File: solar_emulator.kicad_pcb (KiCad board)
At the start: 2 copper layers, 75 parts, among them J1 USB_C_Receptacle, J2 Conn_01x02, J3 Conn_01x03, J4 Conn_01x02, J5 Conn_01x02, J6 Conn_01x04, J7 Conn_01x02, Q1 IRFZ44N, Q2 IRFZ44N, Q3 IRFZ44N, Q4 IRFZ44N, Q5 IRFZ44N, Q6 IRFZ44N, Q7 IRFZ44N, Q8 IRFZ44N, SW1 SW_Push, SW2 SW_Push, U1 ESP32-S3-WROOM-1, U2 LD1117S33TR_SOT223, U3 HIP4081AIPZ, U4 LM393, U5 HIP4081AIPZ, U6 LM393

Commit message: implement footprints, begin placement of components
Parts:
- C2, C3: footprint Capacitor_THT:CP_Radial_D5.0mm_P2.00mm -> Capacitor_THT:C_Disc_D6.0mm_W2.5mm_P5.00mm
- moved C10 270.0 mm to (-162.8, 150.4)
- moved C11 270.0 mm to (-162.8, 154.4)
- moved C5 270.0 mm to (-162.8, 130.2)
- moved C6 270.0 mm to (-162.8, 134.2)
- moved C7 270.0 mm to (-162.8, 138.2)
- moved C8 270.0 mm to (-162.8, 142.3)
- moved C9 270.0 mm to (-162.8, 146.3)
- moved D1 270.0 mm to (-109.3, 130.9)
- moved D2 270.0 mm to (-109.3, 136.3)
- moved D3 270.0 mm to (-109.3, 141.8)
- moved D5 270.0 mm to (-123.1, 130.2)
- moved D6 270.0 mm to (-123.1, 134.5)
- moved D7 270.0 mm to (-123.1, 138.8)
- moved D8 270.0 mm to (-123.1, 143.0)
- moved H1 270.0 mm to (-88.1, 150.0)
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
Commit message: component layout complete, ground plane implemented
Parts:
- removed D1: RED, LED_THT:LED_D3.0mm
- removed D2: GREEN, LED_THT:LED_D3.0mm
- removed D3: BLUE, LED_THT:LED_D3.0mm
- removed D8: 1N5819, Diode_THT:D_DO-41_SOD81_P10.16mm_Horizontal
- removed R1, R2: 5.1k, Resistor_THT:R_Axial_DIN0207_L6.3mm_D2.5mm_P10.16mm_Horizontal
- removed R3: 100, Resistor_THT:R_Axial_DIN0207_L6.3mm_D2.5mm_P10.16mm_Horizontal
- added D4: 1N5819, Diode_THT:D_DO-41_SOD81_P10.16mm_Horizontal, F.Cu at (171.8, 109.2)
- C10: value 1u -> 1n
- C8: value 1n -> 1u
- J1: value USB_C_Receptacle -> USB_C_Receptacle_USB2.0_16P; footprint SparkFun-Connector:USB-C_16 -> Connector_USB:USB_C_Receptacle_HRO_TYPE-C-31-M-12
- J3: value Conn_01x03 -> Conn_01x02; footprint Connector_PinHeader_2.54mm:PinHeader_1x03_P2.54mm_Vertical -> Connector_PinHeader_2.54mm:PinHeader_1x02_P2.54mm_Vertical
- J6: value Conn_01x04 -> Conn_01x03; footprint Connector_PinHeader_2.54mm:PinHeader_1x04_P2.54mm_Vertical -> Connector_PinHeader_2.54mm:PinHeader_1x03_P2.54mm_Vertical
- J7: value Conn_01x02 -> Conn_01x04; footprint Connector_PinHeader_2.54mm:PinHeader_1x02_P2.54mm_Vertical -> Connector_PinHeader_2.54mm:PinHeader_1x04_P2.54mm_Vertical
- R10, R7: value 10k -> 22k
- R11, R12, R14: value 10 -> 10k
- R13: value 10 -> 1k
- R15: value 2.2k -> 1k
- R16: value 1k -> 10k
- R17: value 10k -> 470
- R19, R20: value 22k -> 10
- R21: value 10k -> 10
- R22: value 1k -> 10
- R23: value 10k -> 2.2k
- R24: value 470 -> 2.2k
- R25, R26: value 10 -> 0.1; footprint Resistor_THT:R_Axial_DIN0207_L6.3mm_D2.5mm_P10.16mm_Horizontal -> Resistor_THT:R_Axial_DIN0207_L6.3mm_D2.5mm_P15.24mm_Horizontal
- R27: value 2.2k -> 10
- R28: value 0.1 -> 10; footprint Resistor_THT:R_Axial_DIN0207_L6.3mm_D2.5mm_P15.24mm_Horizontal -> Resistor_THT:R_Axial_DIN0207_L6.3mm_D2.5mm_P10.16mm_Horizontal
- R4, R5: value 100 -> 5.1k
- R6: value 0.1 -> 10k; footprint Resistor_THT:R_Axial_DIN0207_L6.3mm_D2.5mm_P15.24mm_Horizontal -> Resistor_THT:R_Axial_DIN0207_L6.3mm_D2.5mm_P10.16mm_Horizontal
- U4: value LM393 -> HIP4081AIPZ; footprint Package_DIP:DIP-8_W7.62mm -> ul_HIP4081AIPZ:PDIP20_7P11X26P9_INR
- U5: value HIP4081AIPZ -> LM393; footprint ul_HIP4081AIPZ:PDIP20_7P11X26P9_INR -> Package_DIP:DIP-8_W7.62mm
- moved C10 389.5 mm to (223.8, 102.9), turned to 180 degrees
- moved R16 388.0 mm to (238.0, 125.6), turned to 180 degrees
- moved R14 387.4 mm to (237.8, 88.9), turned to 180 degrees
- moved C11 387.1 mm to (224.0, 139.5), turned to 180 degrees
- moved Q6 385.6 mm to (211.1, 83.8), turned to -90 degrees
- moved Q5 384.1 mm to (211.1, 101.6), turned to -90 degrees
- moved Q8 384.0 mm to (211.1, 120.7), turned to -90 degrees
- moved Q7 384.0 mm to (211.1, 138.4), turned to -90 degrees
- moved Q3 377.8 mm to (203.5, 138.4), turned to -90 degrees
- moved Q2 376.4 mm to (203.5, 83.8), turned to -90 degrees
- moved Q4 376.4 mm to (203.5, 120.7), turned to -90 degrees
- moved Q1 376.3 mm to (203.5, 101.6), turned to -90 degrees
- moved R24 375.6 mm to (238.0, 130.6), turned to 180 degrees
- moved R23 374.0 mm to (237.8, 94.0), turned to 180 degrees
- moved R17 373.3 mm to (223.2, 88.9), turned to -90 degrees
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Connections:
- C10 pad 1: Net-(D8-K) -> Net-(U5A-+)
- C10 pad 2: BHS2 -> GND
- C7 pad 1: Net-(D5-K) -> +12V
- C7 pad 2: BHS1 -> GND
- C8 pad 1: Net-(U4A-+) -> Net-(D6-K)
- C8 pad 2: GND -> BHS1
- C9 pad 1: +12V -> Net-(D7-K)
- C9 pad 2: GND -> BHS2
- J2 pad 2: +12V -> LIMIT1
- J3 pad 2: +5V -> +12V
- J5 pad 2: LIMIT1 -> LIMIT2
- J6 pad 1: MOTOR1 -> GND
- J6 pad 2: BHS1 -> +5V
- J6 pad 3: MOTOR3 -> SERVO
- J7 pad 1: GND -> MOTOR1
- J7 pad 2: LIMIT2 -> BHS1
- Q2 pad 1: +12V -> MOTOR1
- Q2 pad 3: BHS1 -> BLS1
- Q4 pad 1: BHS1 -> MOTOR3
- Q4 pad 3: BLS1 -> BLS2
- Q5 pad 1: MOTOR1 -> +12V
- Q5 pad 3: BLS1 -> BHS1
- Q6 pad 1: MOTOR3 -> BHS1
- Q6 pad 3: BLS2 -> BLS1
- R10 pad 1: DIS1 -> Net-(U4-HDEL)
- R11 pad 1: Net-(U3-AHO) -> DIS1
- R11 pad 2: Net-(Q1-G) -> GND
- R12 pad 1: Net-(U3-ALO) -> DIS2
- R12 pad 2: Net-(Q5-G) -> GND
- R13 pad 1: Net-(Q2-G) -> BLS1
- R13 pad 2: BHO1 -> Net-(U5A-+)
- R14 pad 1: Net-(Q4-G) -> +3V3
- R14 pad 2: BLO1 -> Net-(U5A--)
- R15 pad 1: +3V3 -> BLS2
- R15 pad 2: OCP1 -> Net-(U6A-+)
- R16 pad 1: BLS1 -> +3V3
- R16 pad 2: Net-(U4A-+) -> Net-(U6A--)
- R17 pad 1: +3V3 -> GND
- R17 pad 2: Net-(U4A--) -> Net-(U5A--)
- R18 pad 2: Net-(U4A--) -> Net-(U6A--)
- R19 pad 1: Net-(U5-LDEL) -> Net-(U3-AHO)
- R19 pad 2: GND -> Net-(Q1-G)
- R20 pad 1: Net-(U5-HDEL) -> Net-(U3-ALO)
- R20 pad 2: GND -> Net-(Q2-G)
- R21 pad 1: DIS2 -> Net-(U4-AHO)
- R21 pad 2: GND -> Net-(Q3-G)
- R22 pad 1: BLS2 -> Net-(U4-ALO)
- R22 pad 2: Net-(U6A-+) -> Net-(Q4-G)
- R23 pad 2: Net-(U6A--) -> OCP1
- R24 pad 1: GND -> +3V3
- R24 pad 2: Net-(U6A--) -> OCP2
- R25 pad 1: Net-(U5-AHO) -> BLS1
- R25 pad 2: Net-(Q3-G) -> GND
- R26 pad 1: Net-(U5-ALO) -> BLS2
- R26 pad 2: Net-(Q6-G) -> GND
- R27 pad 1: +3V3 -> Net-(Q5-G)
- R27 pad 2: OCP2 -> BHO1
- R28 pad 1: BLS2 -> Net-(Q6-G)
- R28 pad 2: GND -> BLO1
- R4 pad 1: +5V -> Net-(J1-CC2)
- R4 pad 2: Net-(D2-A) -> GND
- R5 pad 1: +12V -> Net-(J1-CC1)
- R5 pad 2: Net-(D3-A) -> GND
- R6 pad 1: BLS1 -> +3V3
- R6 pad 2: GND -> EN
- R7 pad 1: +3V3 -> Net-(U3-LDEL)
- R7 pad 2: EN -> GND
- R8 pad 1: Net-(U3-LDEL) -> Net-(U4-LDEL)
- U3 pad 1: Net-(D5-K) -> Net-(D6-K)
- U3 pad 10: Net-(D6-K) -> Net-(D4-K)
- U4 pad 1: OCP1 -> Net-(D7-K)
- U4 pad 2: Net-(U4A--) -> BHI2
- U4 pad 3: Net-(U4A-+) -> DIS2
- U4 pad 5: (no net) -> BLI2
- U4 pad 6: (no net) -> ALI2
- U4 pad 7: (no net) -> AHI2
- U4 pad 8: +3V3 -> Net-(U4-HDEL)
- U5 pad 1: Net-(D8-K) -> OCP1
- U5 pad 2: BHI2 -> Net-(U5A--)
- U5 pad 3: DIS2 -> Net-(U5A-+)
- U5 pad 5: BLI2 -> (no net)
- U5 pad 6: ALI2 -> (no net)
- U5 pad 7: AHI2 -> (no net)
- U5 pad 8: Net-(U5-HDEL) -> +3V3
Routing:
- added copper zone on B.Cu, net GND
- added copper zone on F.Cu, net GND
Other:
- board outline added: 125.5 x 75 mm

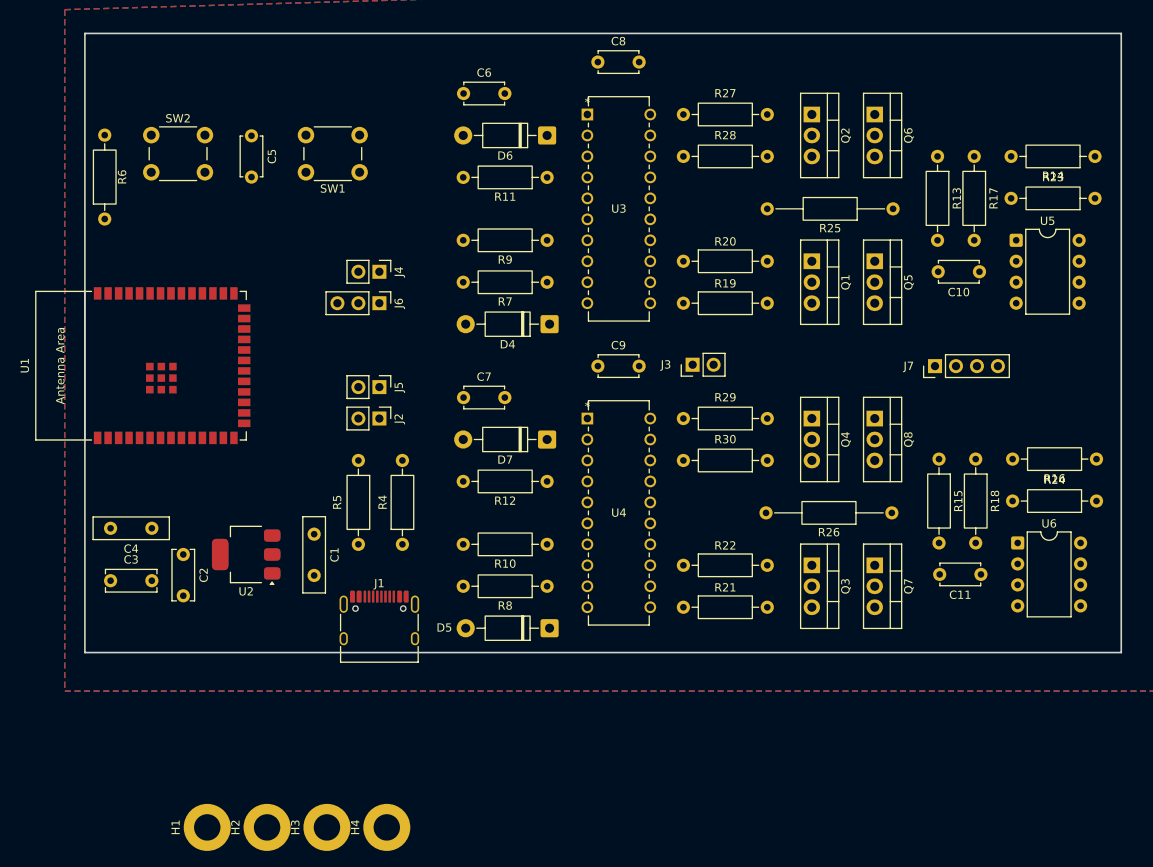
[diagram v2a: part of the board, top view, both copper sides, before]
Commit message: Add traces to power and digital section of pcb
minor rearrangements of components on pcb
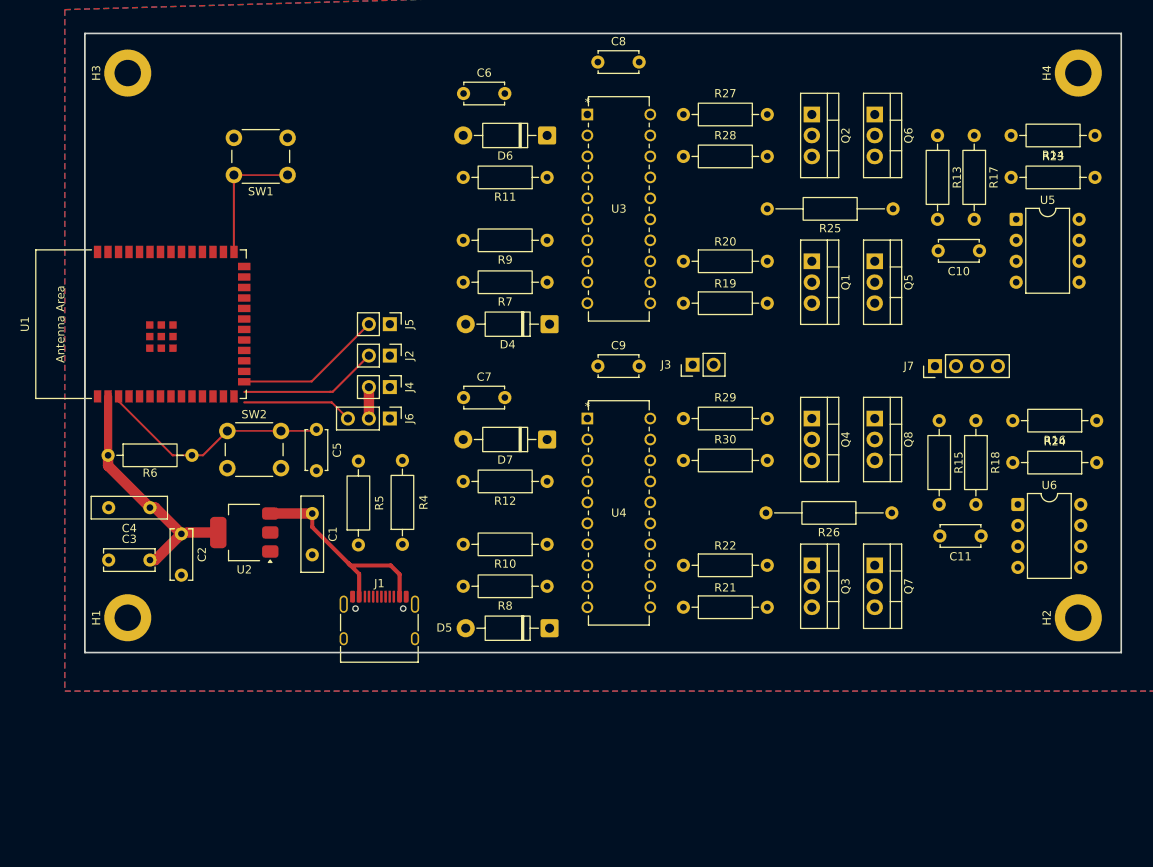
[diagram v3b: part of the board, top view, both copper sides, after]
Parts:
- moved H4 124.0 mm to (235.8, 78.8)
- moved H2 101.5 mm to (235.8, 144.8)
- moved H3 94.5 mm to (120.7, 78.8)
- moved SW2 37.0 mm to (132.7, 122.2)
- moved C5 36.4 mm to (143.5, 122.0)
- moved R6 28.6 mm to (118.3, 125.1), turned to 0 degrees
- moved H1 27.2 mm to (120.7, 144.8)
- moved J4 14.0 mm to (152.4, 116.8)
- moved J6 14.0 mm to (152.4, 120.7)
- moved R5 10.2 mm to (148.6, 136.0), turned to 90 degrees
- moved SW1 8.74 mm to (140.0, 91.2)
- moved J2 7.73 mm to (152.4, 113.0)
- moved J5 7.73 mm to (152.4, 109.2)
- moved U1 5.03 mm to (125.3, 109.2)
- moved C11 4.66 mm to (224.0, 134.9)
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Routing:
- net +3V3: track 0.00 -> 31.7 mm
- net +5V: track 0.00 -> 30.9 mm
- net EN: track 0.00 -> 29.4 mm
- net LIMIT2: track 0.00 -> 18.0 mm
- net LIMIT1: track 0.00 -> 16.9 mm
- net GPIO0: track 0.00 -> 15.8 mm
- net SERVO: track 0.00 -> 13.4 mm

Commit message: add traces to comparator
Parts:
- moved J7 4.48 mm to (214.0, 114.3)
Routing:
- net +3V3: track 31.7 -> 78.8 mm
- net Net-(U6A--): track 0.00 -> 18.3 mm
- net Net-(U5A--): track 0.00 -> 18.3 mm
- net Net-(U6A-+): track 0.00 -> 11.6 mm
- net Net-(U5A-+): track 0.00 -> 11.6 mm
- net Net-(J1-CC1): track 0.00 -> 6.90 mm, vias 0 -> 2
- net Net-(J1-CC2): track 0.00 -> 6.81 mm, vias 0 -> 2
- net OCP2: track 0.00 -> 5.33 mm
- net OCP1: track 0.00 -> 5.33 mm

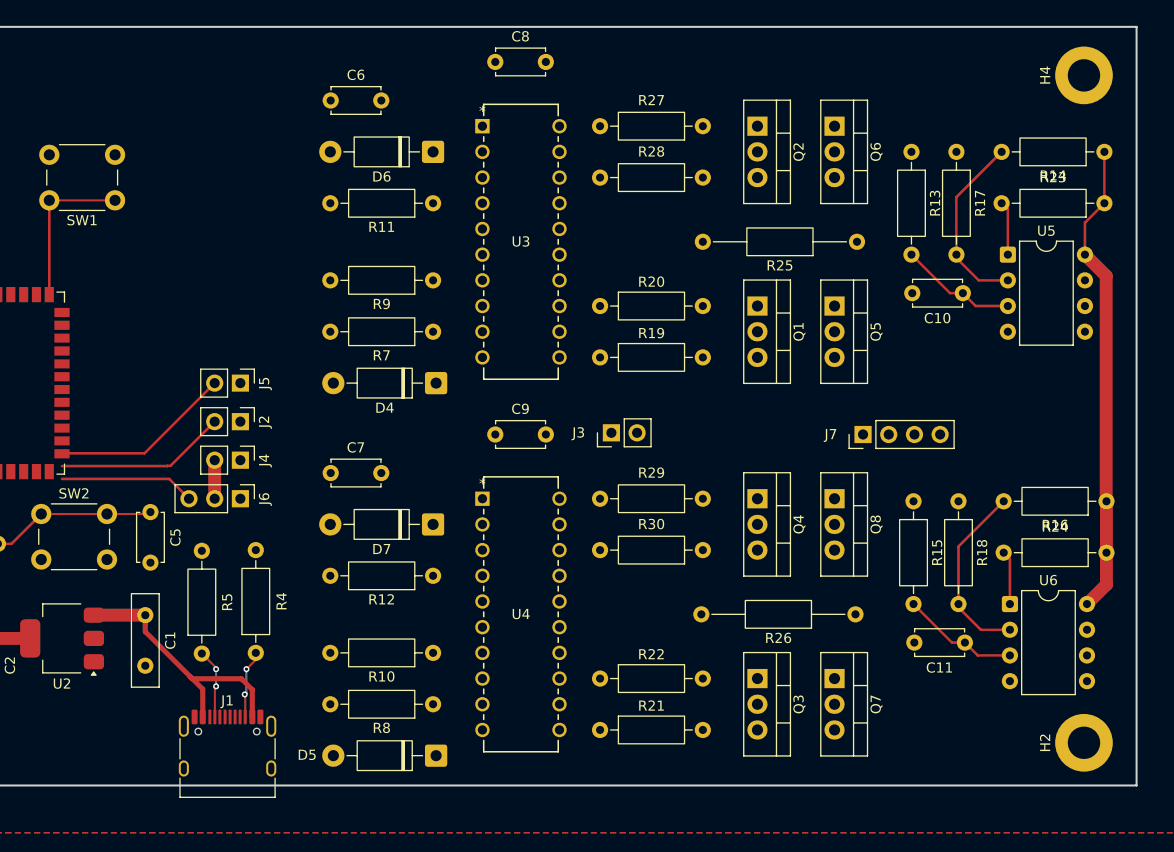
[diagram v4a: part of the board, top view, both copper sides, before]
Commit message: Implement traces to motor sub-circuit
Seek feedback for layout, might need to add copper fill zones
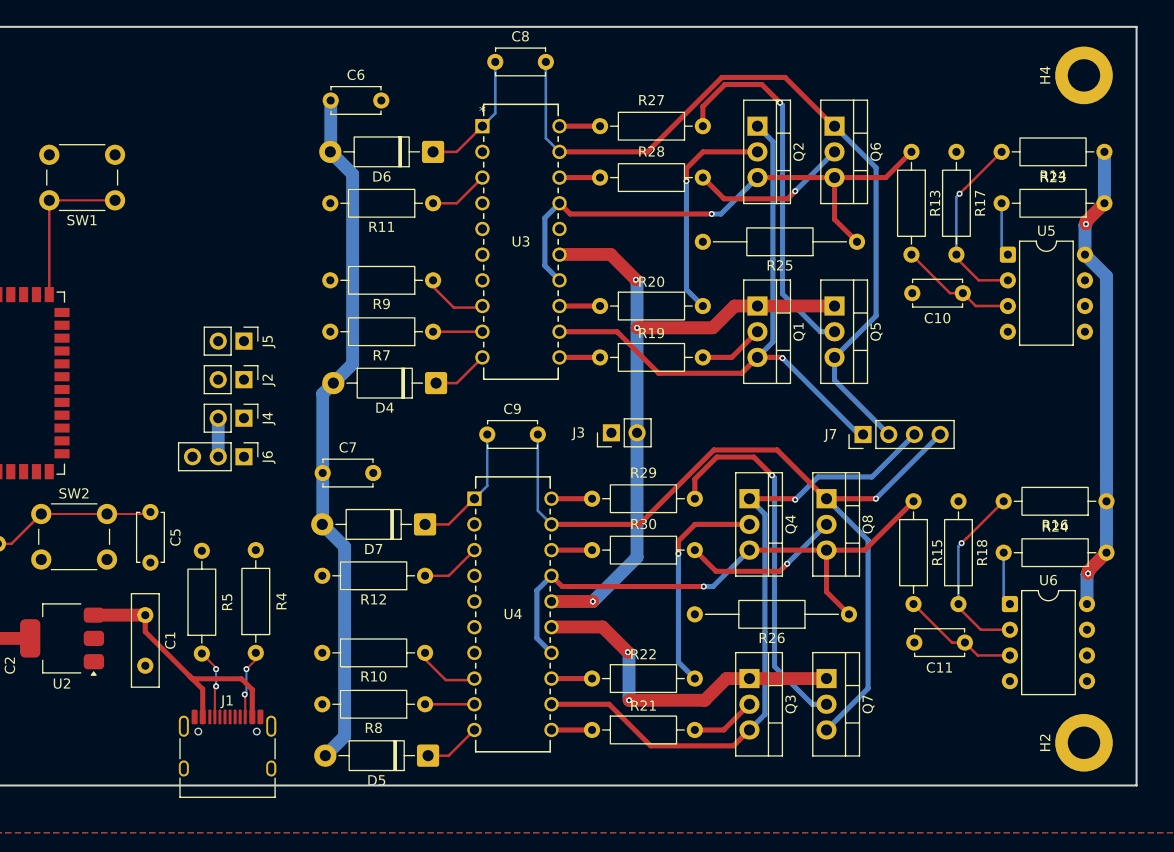
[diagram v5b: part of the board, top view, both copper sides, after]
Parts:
- moved J2 4.16 mm to (152.8, 108.9)
- moved J4 4.16 mm to (152.8, 112.7)
- moved J5 4.16 mm to (152.8, 105.1)
- moved J6 4.16 mm to (152.8, 116.5)
- moved C7 0.79 mm to (160.5, 118.1)
- moved Q3 0.79 mm to (202.7, 138.4)
- moved Q4 0.79 mm to (202.7, 120.7)
- moved R21 0.79 mm to (187.2, 143.5)
- moved R22 0.79 mm to (187.2, 138.4)
- moved R29 0.79 mm to (197.3, 120.7)
- moved R30 0.79 mm to (197.3, 125.7)
- moved U4 0.79 mm to (175.5, 120.7)
- moved C9 0.79 mm to (176.8, 114.3)
- moved D5 0.79 mm to (171.0, 146.1)
- moved D7 0.79 mm to (170.7, 123.2)
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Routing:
- net +12V: track 0.00 -> 169.2 mm, vias 0 -> 5
- net BHS2: track 0.00 -> 81.8 mm, vias 0 -> 1
- net BHS1: track 0.00 -> 77.8 mm
- net MOTOR3: track 0.00 -> 65.1 mm, vias 0 -> 1
- net MOTOR1: track 0.00 -> 59.6 mm, vias 0 -> 1
- net BLS2: track 0.00 -> 55.8 mm, vias 0 -> 1
- net BLS1: track 0.00 -> 53.9 mm, vias 0 -> 1
- net Net-(Q7-G): track 0.00 -> 36.9 mm, vias 0 -> 1
- net Net-(Q5-G): track 0.00 -> 36.9 mm, vias 0 -> 1
- net Net-(Q2-G): track 0.00 -> 22.0 mm, vias 0 -> 1
- net Net-(Q4-G): track 0.00 -> 22.0 mm, vias 0 -> 1
- net LIMIT2: track 18.0 -> 0.00 mm
- net LIMIT1: track 16.9 -> 0.00 mm
- net Net-(Q8-G): track 0.00 -> 15.8 mm, vias 0 -> 1
- net Net-(Q6-G): track 0.00 -> 15.8 mm, vias 0 -> 1
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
